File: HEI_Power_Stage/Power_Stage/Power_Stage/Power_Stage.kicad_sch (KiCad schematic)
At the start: 42 parts, among them IC4 AMC1311DWVR, IC9 ACS730KLCTR-65ABT, J1 Screw_Terminal_01x01, J3 Screw_Terminal_01x01, J4 Screw_Terminal_01x01, J5 Screw_Terminal_01x01, J6 Screw_Terminal_01x01, J8 Conn_02x07_Odd_Even, J9 Conn_02x07_Odd_Even

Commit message: some change
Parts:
- removed D13: PDZVTFTR5.1B, Diode_SMD:D_SOD-128, symbol Device:D_Zener_Small
- added C22: 10nF, Capacitor_SMD:C_0603_1608Metric_Pad1.08x0.95mm_HandSolder, symbol Device:C_Small
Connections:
- net HV-: now also C22.1
- net at IC4.2 (VIN), R16.1, R30.2: now also C22.2
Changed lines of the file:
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@@
 	)
 	(junction
+		(at 297.18 85.09)
+		(diameter 0)
+		(color 0 0 0 0)
+	)
+	(junction
 		(at 207.01 134.62)
 		(diameter 0)
@@
 	)
 	(junction
-		(at 354.33 176.53)
+		(at 297.18 74.93)
 		(diameter 0)
 		(color 0 0 0 0)
@@
 	)
 	(junction
-		(at 354.33 166.37)
-		(diameter 0)
-		(color 0 0 0 0)
-	)
-	(junction
 		(at 304.8 57.15)
 		(diameter 0)
@@
 	(wire
 		(pts
-			(xy 190.5 153.67) (xy 187.96 153.67)
+			(xy 297.18 82.55) (xy 297.18 85.09)
 		)
 		(stroke
@@
 	(wire
 		(pts
-			(xy 217.17 44.45) (xy 217.17 45.72)
+			(xy 190.5 153.67) (xy 187.96 153.67)
 		)
 		(stroke
@@
 	(wire
 		(pts
-			(xy 355.6 173.99) (xy 355.6 176.53)
+			(xy 217.17 44.45) (xy 217.17 45.72)
 		)
 		(stroke
@@
 	(wire
 		(pts
-			(xy 355.6 168.91) (xy 355.6 166.37)
-		)
-		(stroke
-			(width 0)
-			(type default)
-		)
-	)
-	(wire
-		(pts
 			(xy 287.02 74.93) (xy 287.02 76.2)
 		)
@@
 	(wire
 		(pts
-			(xy 297.18 81.28) (xy 297.18 85.09)
+			(xy 303.53 81.28) (xy 303.53 85.09)
 		)
 		(stroke
@@
 	(wire
 		(pts
-			(xy 347.98 166.37) (xy 354.33 166.37)
+			(xy 347.98 166.37) (xy 351.79 166.37)
 		)
 		(stroke
@@
 	(wire
 		(pts
+			(xy 297.18 74.93) (xy 303.53 74.93)
+		)
+		(stroke
+			(width 0)
+			(type default)
+		)
+	)
+	(wire
+		(pts
 			(xy 189.23 81.28) (xy 193.04 81.28)
 		)
@@
 	(wire
 		(pts
+			(xy 297.18 85.09) (xy 303.53 85.09)
+		)
+		(stroke
+			(width 0)
+			(type default)
+		)
+	)
+	(wire
+		(pts
 			(xy 303.53 176.53) (xy 308.61 176.53)
 		)
@@
 	(wire
 		(pts
-			(xy 297.18 81.28) (xy 311.15 81.28)
+			(xy 303.53 81.28) (xy 311.15 81.28)
 		)
 		(stroke
@@
 	(wire
 		(pts
-			(xy 354.33 176.53) (xy 355.6 176.53)
+			(xy 193.04 57.15) (xy 204.47 57.15)
 		)
 		(stroke
@@
 	(wire
 		(pts
-			(xy 193.04 57.15) (xy 204.47 57.15)
+			(xy 287.02 72.39) (xy 287.02 74.93)
 		)
 		(stroke
@@
 	(wire
 		(pts
-			(xy 287.02 72.39) (xy 287.02 74.93)
+			(xy 297.18 74.93) (xy 297.18 77.47)
 		)
 		(stroke
@@
 	(wire
 		(pts
-			(xy 297.18 76.2) (xy 313.69 76.2)
+			(xy 303.53 76.2) (xy 313.69 76.2)
 		)
 		(stroke
@@
 	(wire
 		(pts
-			(xy 297.18 74.93) (xy 297.18 76.2)
+			(xy 303.53 74.93) (xy 303.53 76.2)
 		)
 		(stroke
@@
 	(wire
 		(pts
-			(xy 354.33 166.37) (xy 355.6 166.37)
-		)
-		(stroke
-			(width 0)
-			(type default)
-		)
-	)
-	(wire
-		(pts
-			(xy 354.33 176.53) (xy 347.98 176.53)
+			(xy 347.98 176.53) (xy 351.79 176.53)
 		)
 		(stroke
@@
 	(symbol
 		(lib_id "power:GNDPWR")
-		(at 354.33 176.53 0)
+		(at 351.79 176.53 0)
 		(unit 1)
 		(exclude_from_sim no)
@@
 		(dnp no)
 		(property "Reference" "#PWR028"
-			(at 354.33 181.61 0)
+			(at 351.79 181.61 0)
 			(effects
 				(font
@@
 		)
 		(property "Value" "HV-"
-			(at 356.87 180.34 0)
+			(at 354.33 180.34 0)
 			(effects
 				(font
@@
 		)
 		(property "Footprint" ""
-			(at 354.33 177.8 0)
+			(at 351.79 177.8 0)
 			(effects
 				(font
@@
 		)
 		(property "Datasheet" ""
-			(at 354.33 177.8 0)
+			(at 351.79 177.8 0)
 			(effects
 				(font
@@
 		)
 		(property "Description" ""
-			(at 354.33 176.53 0)
+			(at 351.79 176.53 0)
 			(effects
 				(font
@@
 	)
 	(symbol
+		(lib_id "Device:C_Small")
+		(at 297.18 80.01 180)
+		(unit 1)
+		(exclude_from_sim no)
+		(in_bom yes)
+		(on_board yes)
+		(dnp no)
+		(property "Reference" "C22"
+			(at 294.64 78.232 0)
+			(effects
+				(font
+					(size 1.27 1.27)
+				)
+			)
+		)
+		(property "Value" "10nF"
+			(at 300.736 81.788 0)
+			(effects
+				(font
+					(size 1.27 1.27)
+				)
+			)
+		)
+		(property "Footprint" "Capacitor_SMD:C_0603_1608Metric_Pad1.08x0.95mm_HandSolder"
+			(at 297.18 80.01 0)
+			(effects
+				(font
+					(size 1.27 1.27)
+				)
+				(hide yes)
+			)
+		)
+		(property "Datasheet" "~"
+			(at 297.18 80.01 0)
+			(effects
+				(font
+					(size 1.27 1.27)
+				)
+				(hide yes)
+			)
+		)
+		(property "Description" "Unpolarized capacitor, small symbol"
+			(at 297.18 80.01 0)
+			(effects
+				(font
+					(size 1.27 1.27)
+				)
+				(hide yes)
+			)
+		)
+		(pin "2"
+		)
+		(pin "1"
+		)
+		(instances
+			(project "Power_Stage"
+				(path "/4073579f-dff4-4919-be9b-9c43467e22c1"
+					(reference "C22")
+					(unit 1)
+				)
+			)
+		)
+	)
+	(symbol
 		(lib_id "power:+5V")
 		(at 298.45 55.88 0)
@@
 	(symbol
 		(lib_id "power:+5V")
-		(at 354.33 166.37 0)
+		(at 351.79 166.37 0)
 		(unit 1)
 		(exclude_from_sim no)
@@
 		(dnp no)
 		(property "Reference" "#PWR022"
-			(at 354.33 170.18 0)
+			(at 351.79 170.18 0)
 			(effects
 				(font
@@
 		)
 		(property "Value" "+5V_HV"
-			(at 350.266 162.052 0)
+			(at 347.726 162.052 0)
 			(effects
 				(font
@@
 		)
 		(property "Footprint" ""
-			(at 354.33 166.37 0)
+			(at 351.79 166.37 0)
 			(effects
 				(font
@@
 		)
 		(property "Datasheet" ""
-			(at 354.33 166.37 0)
+			(at 351.79 166.37 0)
 			(effects
 				(font
@@
 		)
 		(property "Description" ""
-			(at 354.33 166.37 0)
+			(at 351.79 166.37 0)
 			(effects
 				(font
@@
 					(unit 1)
 				)
-			)
-		)
-	)
-	(symbol
-		(lib_id "Device:D_Zener_Small")
-		(at 355.6 171.45 270)
-		(unit 1)
-		(exclude_from_sim no)
-		(in_bom yes)
-		(on_board yes)
-		(dnp no)
-		(property "Reference" "D13"
-			(at 351.282 169.418 90)
-			(effects
-				(font
-					(size 1.27 1.27)
-				)
-				(justify left)
-			)
-		)
-		(property "Value" "PDZVTFTR5.1B"
-			(at 357.378 171.45 90)
-			(effects
-				(font
-					(size 1.27 1.27)
-				)
-				(justify left)
-			)
-		)
-		(property "Footprint" "Diode_SMD:D_SOD-128"
-			(at 355.6 171.45 90)
-			(effects
-				(font
-					(size 1.27 1.27)
-				)
-				(hide yes)
-			)
-		)
-		(property "Datasheet" "https://www.rohm.com/datasheet?p=PDZVTF5.1B&dist=Digi-key&media=referral&source=digi-key.com&campaign=Digi-key"
-			(at 355.6 171.45 90)
-			(effects
-				(font
-					(size 1.27 1.27)
-				)
-				(hide yes)
-			)
-		)
-		(property "Description" "  Zener Diode 5.4 V 1 W ±5.88% Surface Mount PMDTM"
-			(at 355.6 171.45 0)
-			(effects
-				(font
-					(size 1.27 1.27)
-				)
-				(hide yes)
-			)
-		)
-		(property "Vbreakdown" "5.4V"
-			(at 358.14 173.736 90)
-			(effects
-				(font
-					(size 1.27 1.27)
-				)
-			)
-		)
-		(pin "1"
-		)
-		(pin "2"
-		)
-		(instances
-			(project "Power_Stage"
-				(path "/4073579f-dff4-4919-be9b-9c43467e22c1"
-					(reference "D13")
-					(unit 1)
-				)

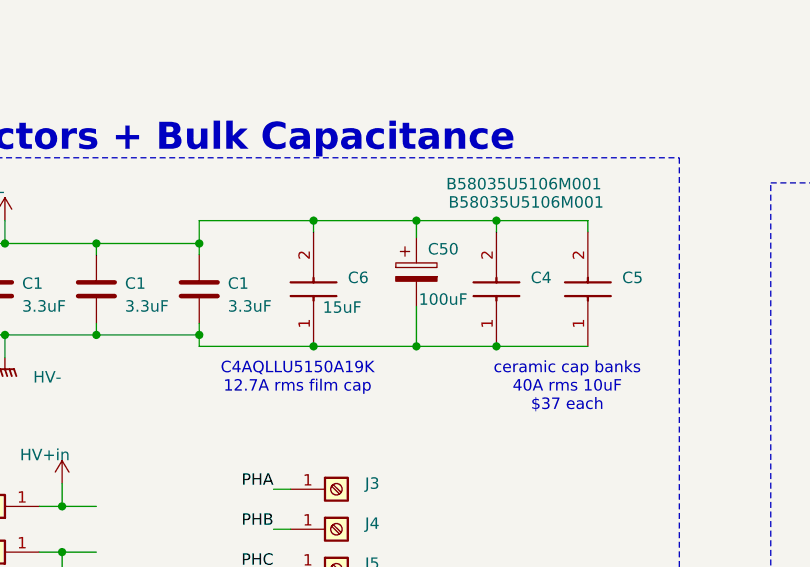
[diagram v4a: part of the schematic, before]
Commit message: all initial placement
initial placement done
routing for one stage done and copied
will make edits and recopy later but wanted to see preview
12.2 x 7.4cm
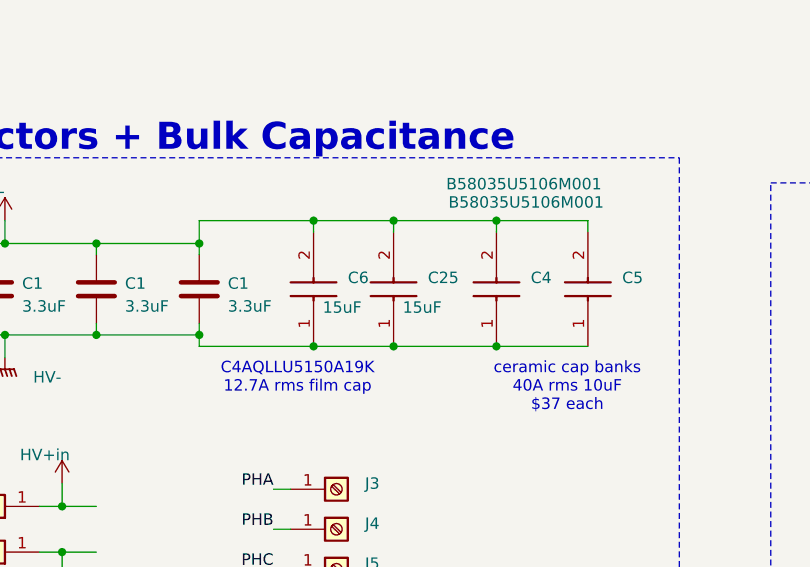
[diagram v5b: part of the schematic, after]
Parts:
- removed C50: 100uF, Capacitor_THT:CP_Radial_D35.0mm_P10.00mm_SnapIn, symbol Device:C_Polarized
- added C25: 15uF, C4AQLLU5150A19K _KiCad:C4AQLLU5150A19K, symbol C4AQLLU5150A19K:C4AQLLU5150A19K
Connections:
- net HV+: now also C25.2
- net HV-: now also C25.1
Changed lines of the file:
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@@
 	)
 	(junction
-		(at 228.6 58.42)
-		(diameter 0)
-		(color 0 0 0 0)
-	)
-	(junction
 		(at 347.98 166.37)
 		(diameter 0)
@@
 	)
 	(junction
+		(at 226.06 58.42)
+		(diameter 0)
+		(color 0 0 0 0)
+	)
+	(junction
 		(at 217.17 58.42)
 		(diameter 0)
@@
 	)
 	(junction
-		(at 237.49 58.42)
+		(at 226.06 44.45)
 		(diameter 0)
 		(color 0 0 0 0)
 	)
 	(junction
-		(at 299.72 129.54)
+		(at 237.49 58.42)
 		(diameter 0)
 		(color 0 0 0 0)
 	)
 	(junction
-		(at 311.15 81.28)
+		(at 299.72 129.54)
 		(diameter 0)
 		(color 0 0 0 0)
 	)
 	(junction
-		(at 228.6 44.45)
+		(at 311.15 81.28)
 		(diameter 0)
 		(color 0 0 0 0)
@@
 	(wire
 		(pts
-			(xy 228.6 58.42) (xy 237.49 58.42)
-		)
-		(stroke
-			(width 0)
-			(type default)
-		)
-	)
-	(wire
-		(pts
 			(xy 212.725 83.185) (xy 214.63 83.185)
 		)
@@
 	(wire
 		(pts
-			(xy 228.6 44.45) (xy 237.49 44.45)
-		)
-		(stroke
-			(width 0)
-			(type default)
-		)
-	)
-	(wire
-		(pts
 			(xy 237.49 58.42) (xy 247.65 58.42)
 		)
@@
 	(wire
 		(pts
+			(xy 226.06 44.45) (xy 226.06 45.72)
+		)
+		(stroke
+			(width 0)
+			(type default)
+		)
+	)
+	(wire
+		(pts
 			(xy 193.04 46.99) (xy 193.04 48.26)
 		)
@@
 	(wire
 		(pts
+			(xy 226.06 58.42) (xy 237.49 58.42)
+		)
+		(stroke
+			(width 0)
+			(type default)
+		)
+	)
+	(wire
+		(pts
 			(xy 237.49 148.59) (xy 234.95 148.59)
 		)
@@
 	(wire
 		(pts
-			(xy 228.6 46.355) (xy 228.6 44.45)
-		)
-		(stroke
-			(width 0)
-			(type default)
-		)
-	)
-	(wire
-		(pts
 			(xy 342.9 170.18) (xy 342.9 166.37)
 		)
@@
 	(wire
 		(pts
+			(xy 226.06 44.45) (xy 237.49 44.45)
+		)
+		(stroke
+			(width 0)
+			(type default)
+		)
+	)
+	(wire
+		(pts
 			(xy 299.72 132.08) (xy 308.61 132.08)
 		)
@@
 	(wire
 		(pts
-			(xy 217.17 58.42) (xy 228.6 58.42)
+			(xy 217.17 58.42) (xy 226.06 58.42)
 		)
 		(stroke
@@
 	(wire
 		(pts
-			(xy 217.17 44.45) (xy 228.6 44.45)
+			(xy 217.17 44.45) (xy 226.06 44.45)
 		)
 		(stroke
@@
 	(wire
 		(pts
-			(xy 228.6 53.975) (xy 228.6 58.42)
-		)
-		(stroke
-			(width 0)
-			(type default)
-		)
-	)
-	(wire
-		(pts
 			(xy 134.62 59.69) (xy 130.81 59.69)
 		)
@@
 	)
 	(symbol
-		(lib_id "Device:C_Polarized")
-		(at 228.6 50.165 0)
-		(unit 1)
-		(exclude_from_sim no)
-		(in_bom yes)
-		(on_board yes)
-		(dnp no)
-		(property "Reference" "C50"
-			(at 229.87 47.625 0)
-			(effects
-				(font
-					(size 1.27 1.27)
-				)
-				(justify left)
-			)
-		)
-		(property "Value" "100uF"
-			(at 228.854 53.213 0)
-			(effects
-				(font
-					(size 1.27 1.27)
-				)
-				(justify left)
-			)
-		)
-		(property "Footprint" "Capacitor_THT:CP_Radial_D35.0mm_P10.00mm_SnapIn"
-			(at 229.5652 53.975 0)
-			(effects
-				(font
-					(size 1.27 1.27)
-				)
-				(hide yes)
-			)
-		)
-		(property "Datasheet" "~"
-			(at 228.6 50.165 0)
-			(effects
-				(font
-					(size 1.27 1.27)
-				)
-				(hide yes)
-			)
-		)
-		(property "Description" "Polarized capacitor"
-			(at 228.6 50.165 0)
-			(effects
-				(font
-					(size 1.27 1.27)
-				)
-				(hide yes)
-			)
-		)
-		(pin "1"
-		)
-		(pin "2"
-		)
-		(instances
-			(project "Power_Stage"
-				(path "/4073579f-dff4-4919-be9b-9c43467e22c1"
-					(reference "C50")
-					(unit 1)
-				)
-			)
-		)
-	)
-	(symbol
 		(lib_id "power:GNDPWR")
 		(at 78.74 152.4 0)
@@
 					(unit 1)
 				)
+			)
+		)
+	)
+	(symbol
+		(lib_id "C4AQLLU5150A19K:C4AQLLU5150A19K")
+		(at 226.06 58.42 90)
+		(unit 1)
+		(exclude_from_sim no)
+		(in_bom yes)
+		(on_board yes)
+		(dnp no)
+		(property "Reference" "C25"
+			(at 229.87 50.7999 90)
+			(effects
+				(font
+					(size 1.27 1.27)
+				)
+				(justify right)
+			)
+		)
+		(property "Value" "15uF"
+			(at 227.076 54.102 90)
+			(effects
+				(font
+					(size 1.27 1.27)
+				)
+				(justify right)
+			)
+		)
+		(property "Footprint" "C4AQLLU5150A19K _KiCad:C4AQLLU5150A19K"
+			(at 322.25 49.53 0)
+			(effects
+				(font
+					(size 1.27 1.27)
+				)
+				(justify left top)
+				(hide yes)
+			)
+		)
+		(property "Datasheet" "https://www.kemet.com/specsheet/C4AQLLU5150A19K"
+			(at 422.25 49.53 0)
+			(effects
+				(font
+					(size 1.27 1.27)
+				)
+				(justify left top)
+				(hide yes)
+			)
+		)
+		(property "Description" "C4AQ, Film, Metallized Polypropylene, Automotive DC Link, 15 uF, 10%, 500 VDC, 105C, -55C, 70C, 2 GOhms, 10 V/us, 16 nH, 28.6 g, 32mm, 19mm, 31mm, Lead Spacing = 27.5mm, 80"
+			(at 226.06 58.42 0)
+			(effects
+				(font
+					(size 1.27 1.27)
+				)
+				(hide yes)
+			)
+		)
+		(property "Height" "19.2"
+			(at 622.25 49.53 0)
+			(effects
+				(font
+					(size 1.27 1.27)
+				)
+				(justify left top)
+				(hide yes)
+			)
+		)
+		(property "Manufacturer_Name" "KEMET"
+			(at 722.25 49.53 0)
+			(effects
+				(font
+					(size 1.27 1.27)
+				)
+				(justify left top)
+				(hide yes)
+			)
+		)
+		(property "Manufacturer_Part_Number" "C4AQLLU5150A19K"
+			(at 822.25 49.53 0)
+			(effects
+				(font
+					(size 1.27 1.27)
+				)
+				(justify left top)
+				(hide yes)
+			)
+		)
+		(property "Mouser Part Number" "80-C4AQLLU5150A19K"
+			(at 922.25 49.53 0)
+			(effects
+				(font
+					(size 1.27 1.27)
+				)
+				(justify left top)
+				(hide yes)
+			)
+		)
+		(property "Mouser Price/Stock" "https://www.mouser.co.uk/ProductDetail/KEMET/C4AQLLU5150A19K?qs=OlC7AqGiEDn77NeU4Ri2AA%3D%3D"
+			(at 1022.25 49.53 0)
+			(effects
+				(font
+					(size 1.27 1.27)
+				)
+				(justify left top)
+				(hide yes)
+			)
+		)
+		(property "Arrow Part Number" ""
+			(at 1122.25 49.53 0)
+			(effects
+				(font
+					(size 1.27 1.27)
+				)
+				(justify left top)
+				(hide yes)
+			)
+		)
+		(property "Arrow Price/Stock" ""
+			(at 1222.25 49.53 0)
+			(effects
+				(font
+					(size 1.27 1.27)
+				)
+				(justify left top)
+				(hide yes)
+			)
+		)
+		(pin "2"
+		)
+		(pin "1"
+		)
+		(instances
+			(project "Power_Stage"
+				(path "/4073579f-dff4-4919-be9b-9c43467e22c1"
+					(reference "C25")
+					(unit 1)
+				)

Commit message: big layout change
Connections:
- net PHAI_{sense} is gone; now on net DCV_{sense}-: J9.1 (Pin_1)
- net PHAI_{sense}ref is gone; now on net DCV_{sense}+: J9.3 (Pin_3)
- net PHBI_{sense} is gone; now on net DCI_{sense}-: J9.5 (Pin_5)
- net AHS_{PWM}: now also J8.2 (Pin_2); no longer J8.1 (Pin_1)
- net ALS_{PWM}: now also J8.4 (Pin_4); no longer J8.3 (Pin_3)
- net BHS_{PWM}: now also J8.6 (Pin_6); no longer J8.5 (Pin_5)
- net BLS_{PWM}: now also J8.8 (Pin_8); no longer J8.7 (Pin_7)
- net CHS_{PWM}: now also J8.10 (Pin_10); no longer J8.9 (Pin_9)
- net CLS_{PWM}: now also J8.12 (Pin_12); no longer J8.11 (Pin_11)
- net PHCI_{sense}+: now reaches J9.10 (Pin_10)
- net PHCI_{sense}-: now reaches J9.12 (Pin_12)
- net DCI_{sense} renamed PHAI_{sense}+
- net DCI_{sense}A renamed DCI_{sense}+
- net DCI_{sense}+: now also J9.7 (Pin_7)
- net DCI_{sense}ref renamed DCI_{sense}-
- net DCI_{sense}-: no longer J9.4 (Pin_4)
- net DCV_{sense}M renamed DCV_{sense}-
- net DCV_{sense}-: no longer J9.6 (Pin_6)
- net DCV_{sense}P renamed DCV_{sense}+
- net DCV_{sense}+: no longer J9.8 (Pin_8)
- net PHBI_{sense}ref: no longer names the net of J9.11 (Pin_11)
- net PHBI_{sense}ref: no longer J9.7 (Pin_7)
- net PHCI_{sense}: no longer names the net of J9.9 (Pin_9)
- new net PHAI_{sense}-: J9.4 (Pin_4)
- new net PHBI_{sense}+: J9.6 (Pin_6)
- new net PHBI_{sense}-: J9.8 (Pin_8)
- no-connect marks 8 -> 0
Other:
- sheet Phase1 ports: added PH_{Isense}+, PH_{Isense}-; removed PH_{Isense}, PH_{Isense}ref
- sheet Phase2 ports: added PH_{Isense}+, PH_{Isense}-; removed PH_{Isense}, PH_{Isense}ref
- sheet Phase3 ports: added PH_{Isense}+, PH_{Isense}-; removed PH_{Isense}, PH_{Isense}ref

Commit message: almost complete routing
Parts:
- removed J6: Screw_Terminal_01x01, GTSR:CONN6_1057_WRE, symbol Connector:Screw_Terminal_01x01
- added J2: Screw_Terminal_01x01, MountingHole:MountingHole_4.3mm_M4_Pad, symbol Connector:Screw_Terminal_01x01
- J1, J3, J4, J5: footprint GTSR:CONN6_1057_WRE -> MountingHole:MountingHole_4.3mm_M4_Pad
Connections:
- net HV+in: now also J4.1 (Pin_1); no longer J1.1 (Pin_1), J1.2 (Pin_1), J1.3 (Pin_1), J1.4 (Pin_1), J1.5 (Pin_1), J1.6 (Pin_1)
- net HV-: now also J5.1 (Pin_1)
- net PHA: now also J2.1 (Pin_1); no longer J3.1 (Pin_1), J3.2 (Pin_1), J3.3 (Pin_1), J3.4 (Pin_1), J3.5 (Pin_1), J3.6 (Pin_1)
- net PHB: now also J1.1 (Pin_1); no longer J4.1 (Pin_1), J4.2 (Pin_1), J4.3 (Pin_1), J4.4 (Pin_1), J4.5 (Pin_1), J4.6 (Pin_1)
- net PHC: now also J3.1 (Pin_1); no longer J5.1 (Pin_1), J5.2 (Pin_1), J5.3 (Pin_1), J5.4 (Pin_1), J5.5 (Pin_1), J5.6 (Pin_1)

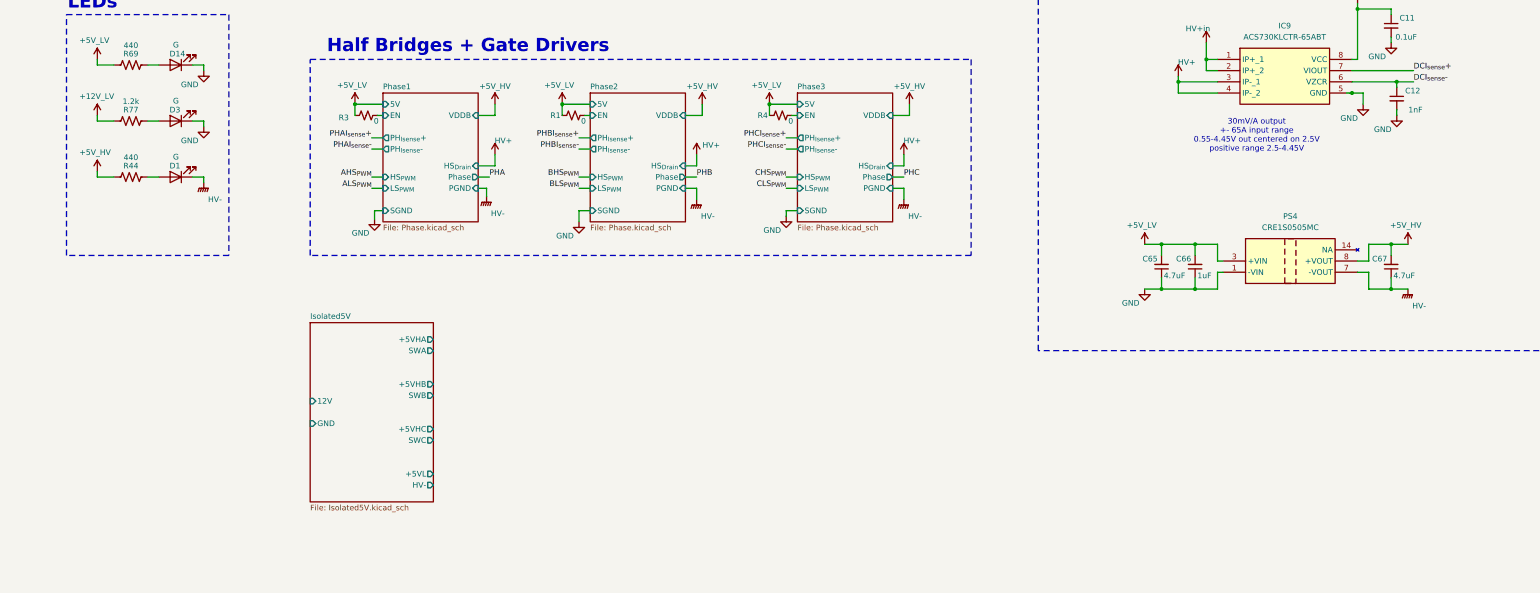
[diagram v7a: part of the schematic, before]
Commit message: allegro gate driver version schematic overhall and layout
layout and routing almost complete for allegro gate drivers
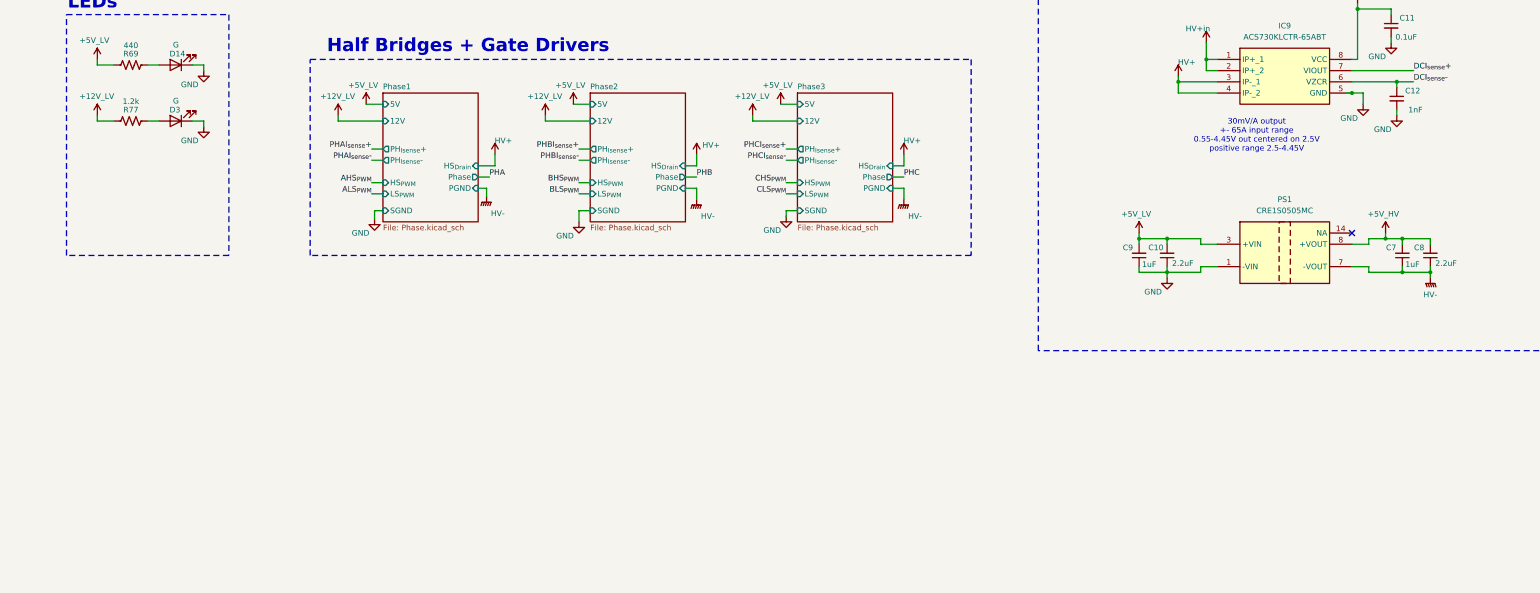
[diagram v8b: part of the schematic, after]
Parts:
- removed C65, C67: 4.7uF, Capacitor_SMD:C_0603_1608Metric_Pad1.08x0.95mm_HandSolder, symbol Device:C_Small
- removed C66: 1uF, Capacitor_SMD:C_0603_1608Metric_Pad1.08x0.95mm_HandSolder, symbol Device:C_Small
- removed D1: G, LED_SMD:LED_0603_1608Metric_Pad1.05x0.95mm_HandSolder, symbol Device:LED
- removed PS4: CRE1S0505MC, CRE1S0505MC_KiCad:CRE1S0505MC, symbol CRE1S0505MC:CRE1S0505MC
- removed R1, R3, R4: 0, Resistor_SMD:R_0603_1608Metric_Pad0.98x0.95mm_HandSolder, symbol Device:R_Small_US
- removed R44: 440, Resistor_SMD:R_0603_1608Metric_Pad0.98x0.95mm_HandSolder, symbol Device:R_US
- added C10, C8: 2.2uF, Capacitor_SMD:C_0603_1608Metric_Pad1.08x0.95mm_HandSolder, symbol Device:C_Small
- added C7, C9: 1uF, Capacitor_SMD:C_0603_1608Metric_Pad1.08x0.95mm_HandSolder, symbol Device:C_Small
- added PS1: CRE1S0505MC, CRE1S0505MC, symbol CRE1S0505MC:CRE1S0505MC
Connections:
- net +5V_HV: now also C7.2, C8.2, PS1.8 (+VOUT)
- net +5V_LV: now also C10.2, C9.2, PS1.3 (+VIN)
- net GND: now also C10.1, C9.1, PS1.1 (-VIN)
- net HV-: now also C7.1, C8.1, PS1.7 (-VOUT)
- no-connect marks 0 -> 1
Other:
- removed sheet Isolated5V
- sheet Phase1 ports: added 12V; removed EN, VDDB
- sheet Phase2 ports: added 12V; removed EN, VDDB
- sheet Phase3 ports: added 12V; removed EN, VDDB
